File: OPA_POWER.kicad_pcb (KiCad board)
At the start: 4 copper layers, 110 x 80 mm, 204 parts, among them J1 Conn_01x02, J10 Conn_02x14_Odd_Even, J11 Conn_01x04, J18 Conn_01x01, J19 Conn_01x01, J2 Jumper, J3 Jumper, J4 Jumper, J5 Jumper, J6 Jumper, J7 Jumper, J8 Jumper, J9 Conn_01x04, Q1 AO3400, Q2 AO3401, Q3 AO3400, Q4 AO3401, U1 XC6206, U10 LM337, U11 TPS7A2425, U12 TPS72325, U13 TPS7A39, U14 ADP7118(ADJ), U2 MP2333H, U3 ADP5071AREZ-R7, U4 LM2991S, U5 LM2940-9, U6 TPS7A30, U7 TPS7A49, U8 TPS65133, U9 LM317

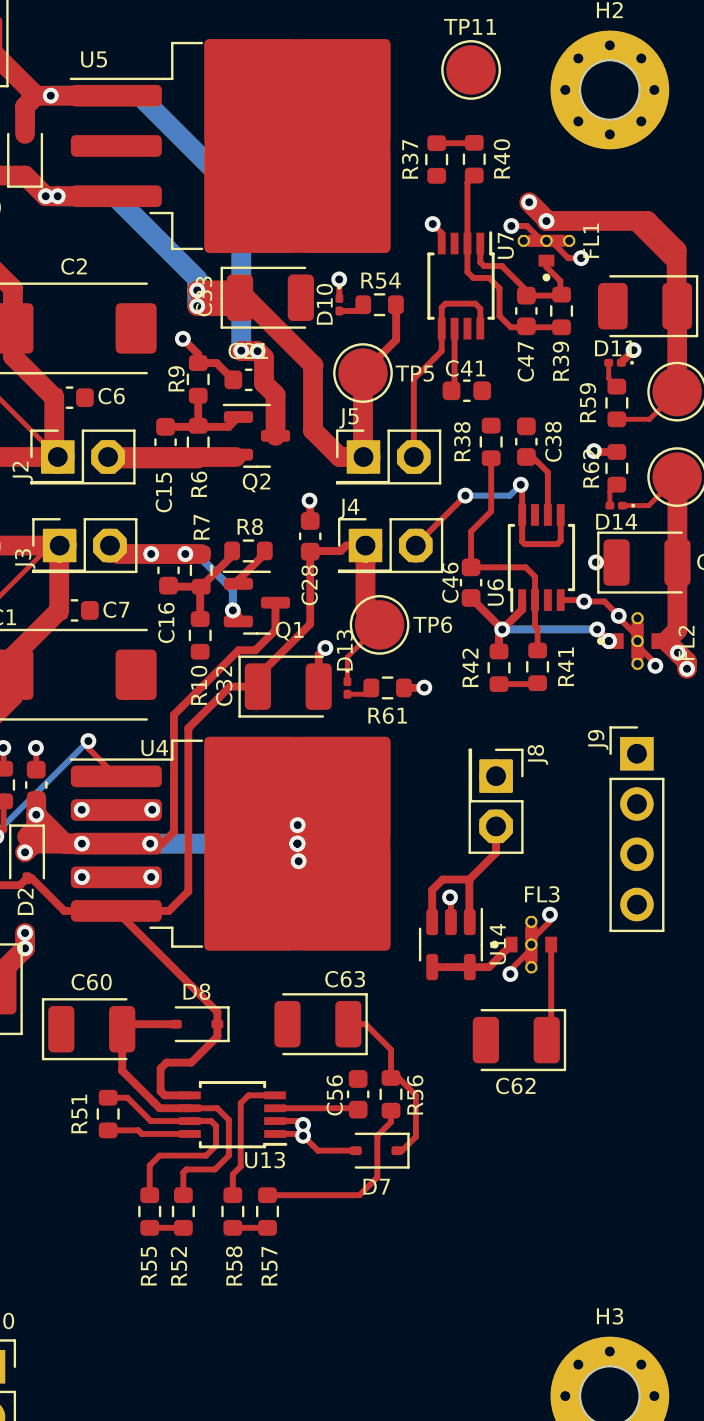
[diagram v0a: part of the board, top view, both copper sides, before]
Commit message: 更新預覽圖
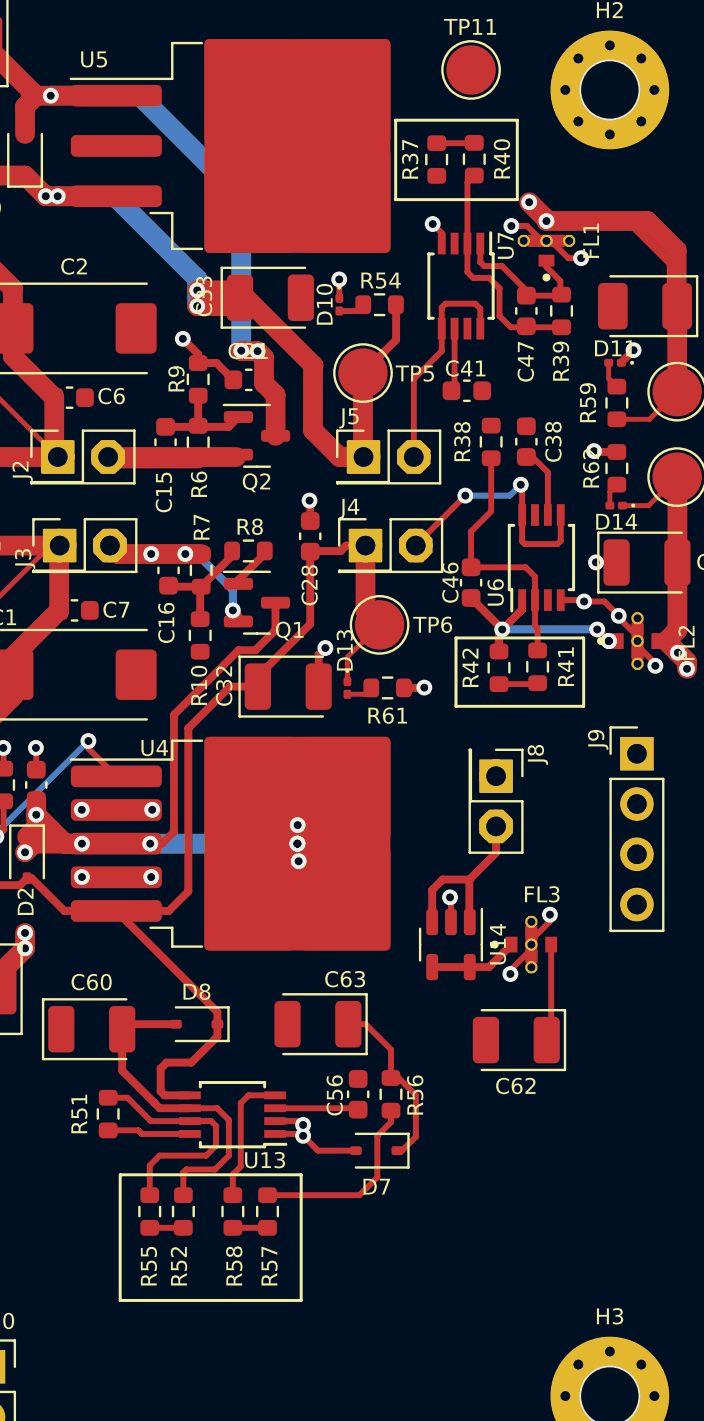
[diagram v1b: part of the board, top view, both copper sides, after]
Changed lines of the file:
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@@
     (property "Sheetfile" "OPA_POWER.kicad_sch")
     (property "Sheetname" "")
-    (attr through_hole)
+    (attr through_hole exclude_from_pos_files)
     (fp_text reference "J7" (at -0.677 -1.936) (layer "F.SilkS")
         (effects (font (size 0.8 0.8) (thickness 0.15)))
@@
     (property "Sheetfile" "OPA_POWER.kicad_sch")
     (property "Sheetname" "")
-    (attr through_hole)
+    (attr through_hole exclude_from_pos_files)
     (fp_text reference "J6" (at -0.712 -2.032) (layer "F.SilkS")
         (effects (font (size 0.8 0.8) (thickness 0.15)))
@@
     (property "Sheetfile" "OPA_POWER.kicad_sch")
     (property "Sheetname" "")
-    (attr through_hole)
+    (attr through_hole exclude_from_pos_files)
     (fp_text reference "J8" (at -1.141 -2.04 90) (layer "F.SilkS")
         (effects (font (size 0.8 0.8) (thickness 0.15)))
@@
     (property "Sheetfile" "OPA_POWER.kicad_sch")
     (property "Sheetname" "")
-    (attr through_hole)
+    (attr through_hole exclude_from_pos_files)
     (fp_text reference "J4" (at -0.762 -1.936) (layer "F.SilkS")
         (effects (font (size 0.8 0.8) (thickness 0.15)))
@@
     (property "ki_description" "Generic connector, single row, 01x02, script generated (kicad-library-utils/schlib/autogen/connector/)")
     (property "ki_keywords" "connector")
-    (attr through_hole)
+    (attr through_hole exclude_from_pos_files)
     (fp_text reference "J1" (at -2.032 -0.757 -90) (layer "F.SilkS")
         (effects (font (size 0.8 0.8) (thickness 0.15)))
@@
     (property "ki_description" "Generic connector, single row, 01x04, script generated (kicad-library-utils/schlib/autogen/connector/)")
     (property "ki_keywords" "connector")
-    (attr through_hole)
+    (attr through_hole exclude_from_pos_files)
     (fp_text reference "J9" (at -2.032 -0.772 -90) (layer "F.SilkS")
         (effects (font (size 0.8 0.8) (thickness 0.15)))
@@
     (property "ki_description" "Generic connector, double row, 02x14, odd/even pin numbering scheme (row 1 odd numbers, row 2 even numbers), script generated (kicad-library-utils/schlib/autogen/connector/)")
     (property "ki_keywords" "connector")
-    (attr through_hole)
+    (attr through_hole exclude_from_pos_files)
     (fp_text reference "J10" (at -2.286 -0.508 -180) (layer "F.SilkS")
         (effects (font (size 0.8 0.8) (thickness 0.15)))
@@
     (property "Sheetfile" "OPA_POWER.kicad_sch")
     (property "Sheetname" "")
-    (attr through_hole)
+    (attr through_hole exclude_from_pos_files)
     (fp_text reference "J2" (at -1.8492 0.635 90) (layer "F.SilkS")
         (effects (font (size 0.8 0.8) (thickness 0.15)))
@@
     (property "ki_description" "Generic connector, single row, 01x04, script generated (kicad-library-utils/schlib/autogen/connector/)")
     (property "ki_keywords" "connector")
-    (attr through_hole)
+    (attr through_hole exclude_from_pos_files)
     (fp_text reference "J11" (at -2.032 -0.01 90) (layer "F.SilkS")
         (effects (font (size 0.8 0.8) (thickness 0.15)))
@@
     (property "Sheetfile" "OPA_POWER.kicad_sch")
     (property "Sheetname" "")
-    (attr through_hole)
+    (attr through_hole exclude_from_pos_files)
     (fp_text reference "J5" (at -0.6622 -2.032) (layer "F.SilkS")
         (effects (font (size 0.8 0.8) (thickness 0.15)))
@@
     (property "Sheetfile" "OPA_POWER.kicad_sch")
     (property "Sheetname" "")
-    (attr through_hole)
+    (attr through_hole exclude_from_pos_files)
     (fp_text reference "J3" (at -1.818 0.604 90) (layer "F.SilkS")
         (effects (font (size 0.8 0.8) (thickness 0.15)))
@@
     )
   )
+  (gr_rect (start 149.658 29.4) (end 155.8048 33.4132)
+    (stroke (width 0.15) (type default)) (fill none) (layer "F.SilkS"))
+  (gr_rect (start 135.7388 82.6892) (end 144.8828 89.0392)
+    (stroke (width 0.15) (type default)) (fill none) (layer "F.SilkS"))
+  (gr_rect (start 152.706 55.562) (end 159.1576 59.0164)
+    (stroke (width 0.15) (type default)) (fill none) (layer "F.SilkS"))
   (gr_circle (center 160.4798 27.8701) (end 161.9798 27.8701)
     (stroke (width 0.1) (type solid)) (fill none) (layer "Edge.Cuts"))

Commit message: 更新庫＂
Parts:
- C1, C29, C31: value Cap Pol1 -> 10uF
- C10, C14: value Cap -> 47nF
- C11: value Cap -> 1nF
- C12, C15, C16, C23, C25, C3, C39, C40, C57: value Cap -> 1uF
- C13: value Cap -> 6.8nF
- C19, C2, C20, C32, C33, C62: value Cap Pol1 -> Cap Pol1 10uF
- C21, C22, C28, C30, C34, C35, C36, C37, C50, C51, C6, C7, C8: value Cap -> 0.1uF
- C24: value Cap -> 10pF
- C26, C27, C5: value Cap Pol1 -> Cap Pol1 22uF
- C38, C41, C46, C47, C56, C58: value Cap -> 10nF
- C42, C43, C52, C53, C54, C55, C60, C63: value Cap Pol1 -> Cap Pol1 4.7uF
- C44, C45: value Tan -> Tan 10uF
- C48, C49: value Cap -> Cap NA
- C59, C61: value Cap -> 2.2uF
- L1, L2: value Inductor -> 2.2uH
- L3: value Inductor -> 10uH
- L4: value Inductor -> 0.47uH
- L7: value Inductor -> 4.7uH
- R1: value Res1 -> 200K
- R10, R31, R32, R9: value Res1 -> 20K
- R11, R39, R51, R58: value Res1 -> 10K
- R12: value Res1 -> 20R
- R13: value Res1 -> 7.68K
- R14, R17, R3, R35, R36: value Res1 -> 4.7K
- R15: value Res1 -> 40.2K
- R18: value Res1 -> 22K
- R19: value Res1 -> 2K
- R2, R20: value Res1 -> 100K
- R21: value Res1 -> 191K
- R22: value Res1 -> 250R
- R23, R42: value Res1 -> 30K
- R24: value Res1 -> 4R
- R25: value Res1 -> 4.42R
- R26, R27, R4, R6, R7: value Res1 -> 470K
- R28, R29, R33, R34, R57, R63, R64: value Res1 -> 0R
- R37: value Res1 -> 106R
- R40: value Res1 -> 3K
- R41: value Res1 -> 2.4K
- R45, R46, R47, R48, R49, R50: value Res1 -> NA
- R5: value Res1 -> 15K
- R52: value Res1 -> 40K
- R55: value Res1 -> 2.2K
- R56: value Res1 -> 32.4K
- R8: value Res1 -> 1K
